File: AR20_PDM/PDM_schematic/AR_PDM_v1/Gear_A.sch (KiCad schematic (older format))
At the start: 18 parts, among them Q1 BTS50025-1TAD, U1 INA233

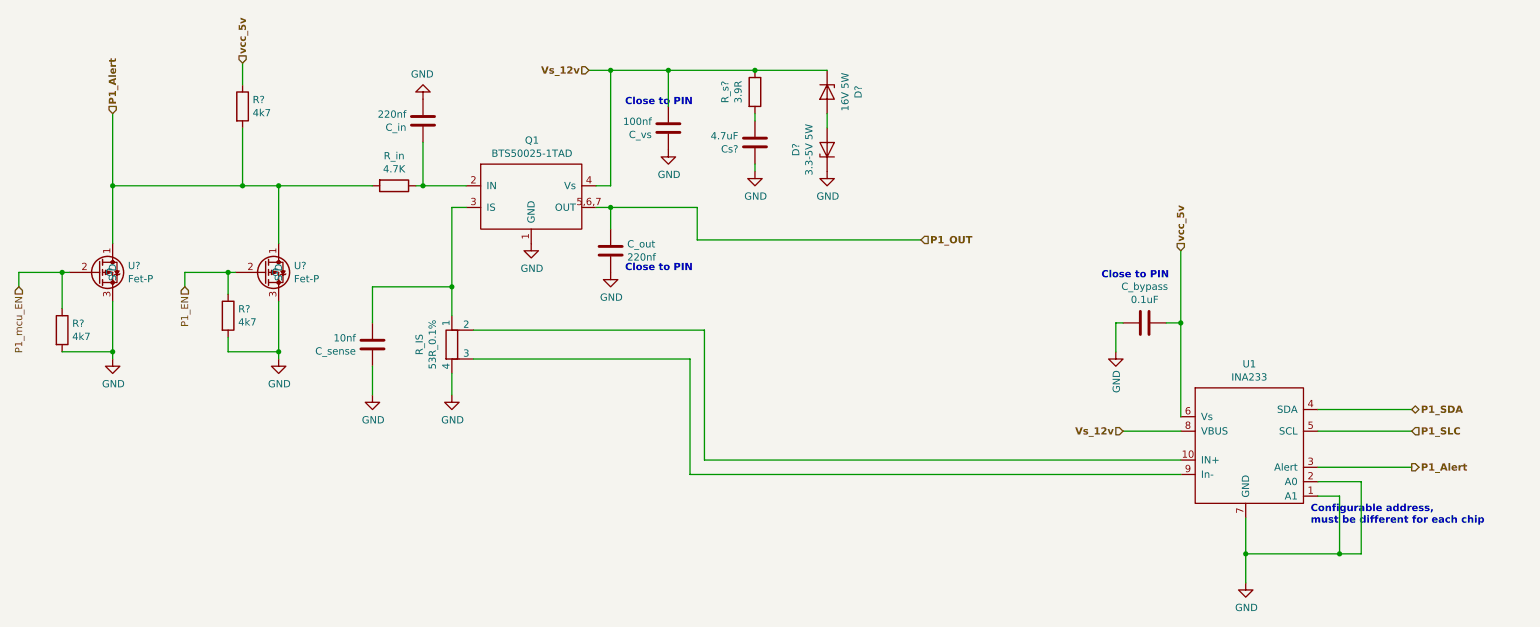
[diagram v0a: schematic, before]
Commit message: First draft of Gear phase, shutdown relays, and Direct phases.
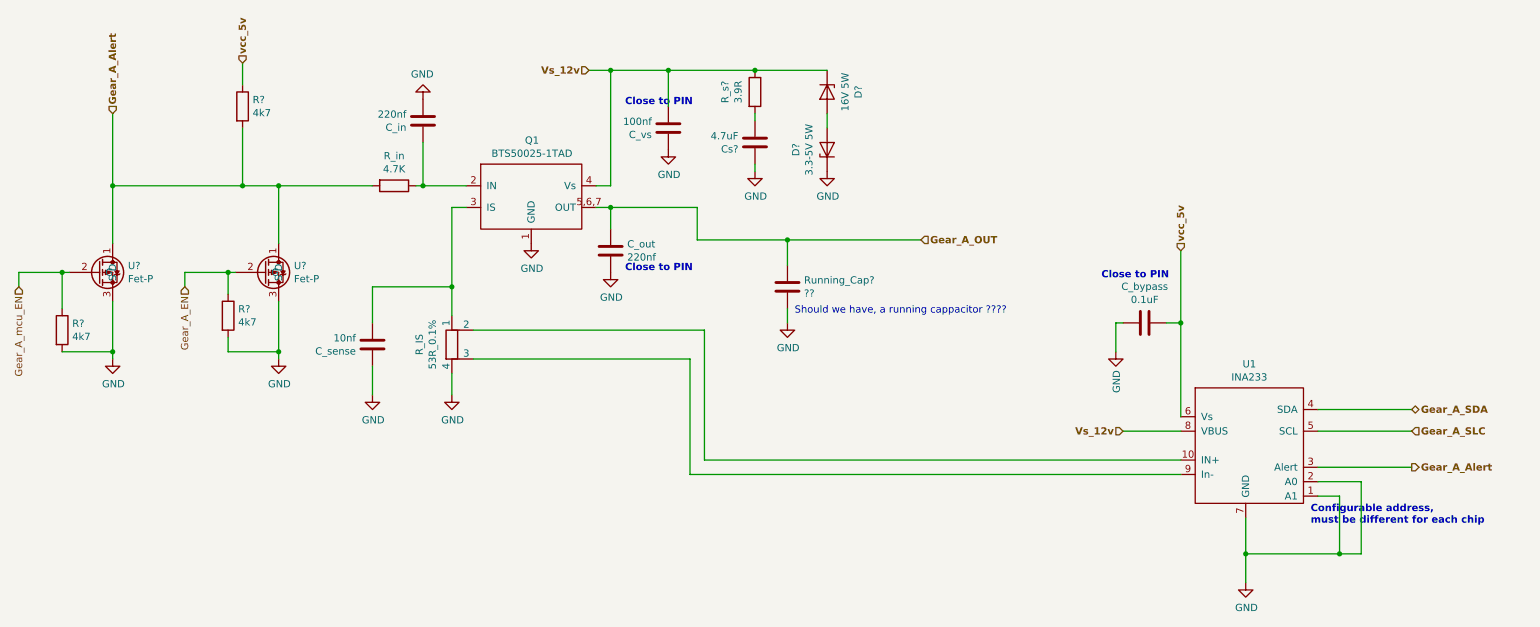
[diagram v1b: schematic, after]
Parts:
- added Running_Cap?: ??, symbol AR20_PDM_v1-rescue:C-Device
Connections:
- net GND: now also Running_Cap?.2
- net P1_Alert renamed Gear_A_Alert
- net P1_EN renamed Gear_A_EN
- net P1_OUT renamed Gear_A_OUT
- net Gear_A_OUT: now also Running_Cap?.1
- net P1_SDA renamed Gear_A_SDA
- net P1_SLC renamed Gear_A_SLC
- net P1_mcu_EN renamed Gear_A_mcu_EN
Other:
- note added: "Should we have, a running cappacitor ????\n\n"
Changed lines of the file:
@@
 vcc_5v
 Text HLabel 10350 4350 2    50   Output ~ 10
-P1_Alert
+Gear_A_Alert
 Text HLabel 10350 3950 2    50   BiDi ~ 10
-P1_SDA
+Gear_A_SDA
 Text HLabel 10350 4100 2    50   Input ~ 10
-P1_SLC
+Gear_A_SLC
 Text Notes 4900 3000 0    50   ~ 10
 Close to PIN
@@
 	2250 1550 2250 1700
 Text HLabel 6950 2775 2    50   Input ~ 10
-P1_OUT
+Gear_A_OUT
 $Comp
 L AR20_PDM_v1-rescue:C-Device C_vs
@@
 	5350 3600 5350 4400
 Text HLabel 1350 1900 1    50   Input ~ 10
-P1_Alert
+Gear_A_Alert
 Wire Wire Line
 	9700 4350 10350 4350
@@
 Connection ~ 1000 3000
 Text HLabel 700  3100 3    50   Input ~ 0
-P1_mcu_EN
+Gear_A_mcu_EN
 Wire Wire Line
 	700  3000 700  3100
@@
 	1850 3100 1850 3000
 Text HLabel 1850 3100 3    50   Input ~ 0
-P1_EN
+Gear_A_EN
 Connection ~ 2150 3000
 Wire Wire Line
@@
 	5400 2550 5400 2775
 Wire Wire Line
-	5400 2775 6950 2775
+	5400 2775 6025 2775
 Connection ~ 4800 2550
 Wire Wire Line
@@
 Wire Wire Line
 	6300 1900 6300 2000
+$Comp
+L AR20_PDM_v1-rescue:C-Device Running_Cap?
+U 1 1 5DEC8229
+P 6025 3100
+AR Path="/5DA89415/5DEC8229" Ref="Running_Cap?"  Part="1"
+AR Path="/5DEB10A1/5DEC8229" Ref="Running_Cap?"  Part="1"
+AR Path="/5DEB20EA/5DEC8229" Ref="Running_Cap?"  Part="1"
+F 0 "Running_Cap?" H 6140 3146 50  0000 L CNN
+F 1 "??" H 6140 3055 50  0000 L CNN
+F 2 "" H 6063 2950 50  0001 C CNN
+F 3 "~" H 6025 3100 50  0001 C CNN
+	1    6025 3100
+	1    0    0    -1
+$EndComp
+$Comp
+L AR20_PDM_v1-rescue:GND-power #PWR?
+U 1 1 5DEC822F
+P 6025 3350
+AR Path="/5DA89415/5DEC822F" Ref="#PWR?"  Part="1"
+AR Path="/5DEB10A1/5DEC822F" Ref="#PWR?"  Part="1"
+AR Path="/5DEB20EA/5DEC822F" Ref="#PWR?"  Part="1"
+F 0 "#PWR?" H 6025 3100 50  0001 C CNN
+F 1 "GND" H 6030 3177 50  0000 C CNN
+F 2 "" H 6025 3350 50  0001 C CNN
+F 3 "" H 6025 3350 50  0001 C CNN
+	1    6025 3350
+	1    0    0    -1
+$EndComp
+Wire Wire Line
+	6025 3350 6025 3250
+Text Notes 6075 3375 0    50   ~ 0
+Should we have, a running cappacitor ????\n\n
+Wire Wire Line
+	6025 2775 6025 2950
+Connection ~ 6025 2775
+Wire Wire Line
+	6025 2775 6950 2775
 $EndSCHEMATC

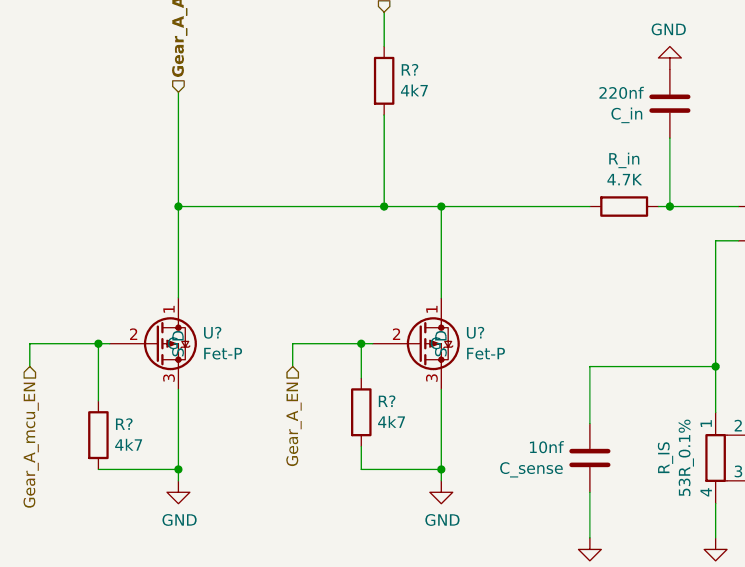
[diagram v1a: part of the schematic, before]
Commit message: Added label on mosfets, added fuel pump sinking output
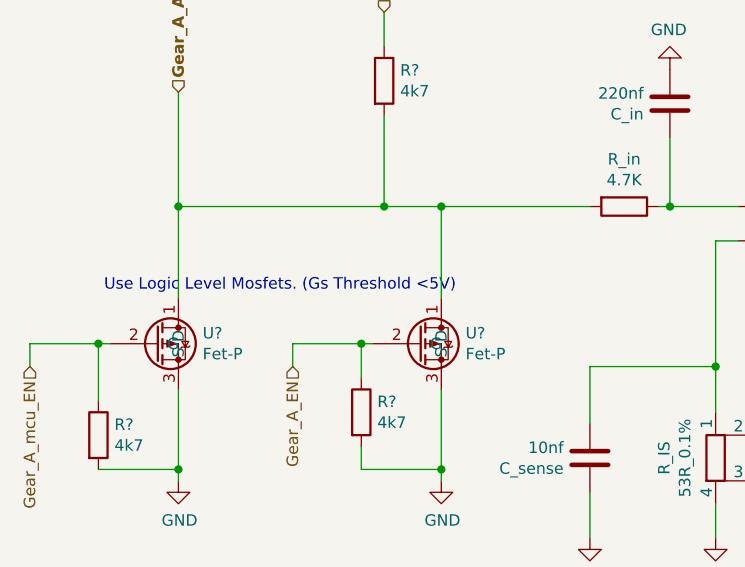
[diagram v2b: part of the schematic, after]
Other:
- note added: "Use Logic Level Mosfets. (Gs Threshold <5V)"
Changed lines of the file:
@@
 Wire Wire Line
 	6025 2775 6950 2775
+Text Notes 1025 2775 0    50   ~ 0
+Use Logic Level Mosfets. (Gs Threshold <5V)
 $EndSCHEMATC
